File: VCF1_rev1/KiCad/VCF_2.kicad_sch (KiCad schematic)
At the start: 41 parts, among them U3 CEM3350, U4 Opamp_Quad, U5 74HC4053, U6 LM13700

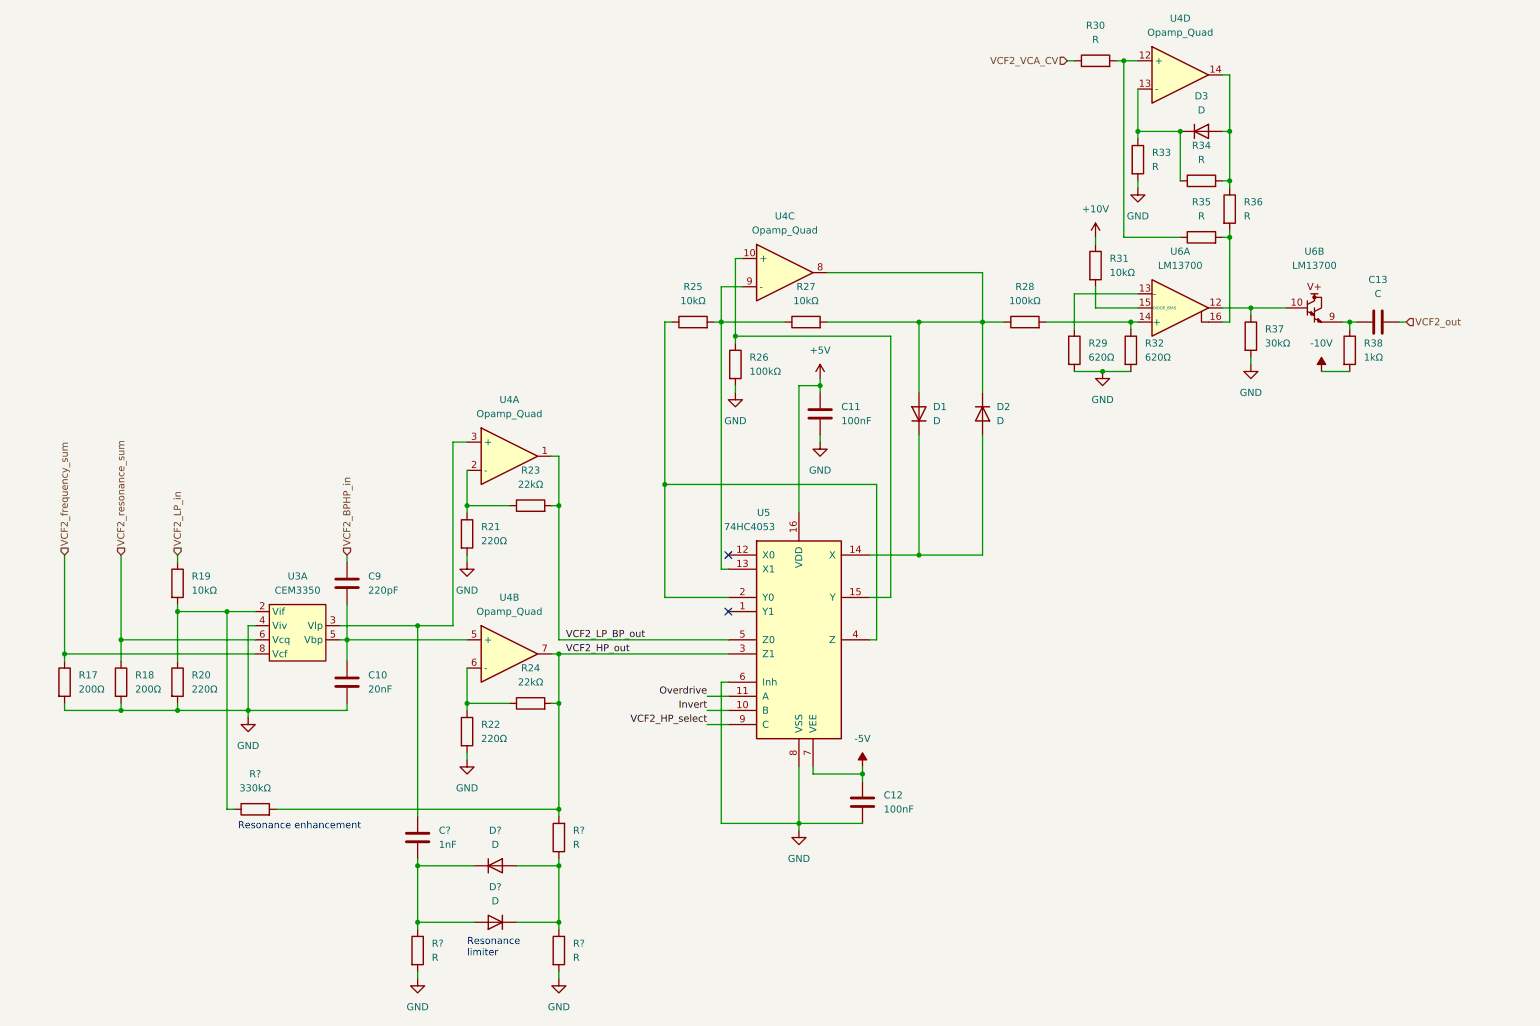
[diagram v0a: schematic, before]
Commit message: Added VCA (with a quirk) and also drew a new symbol for 74HC4053 because the standard one annoyed me.
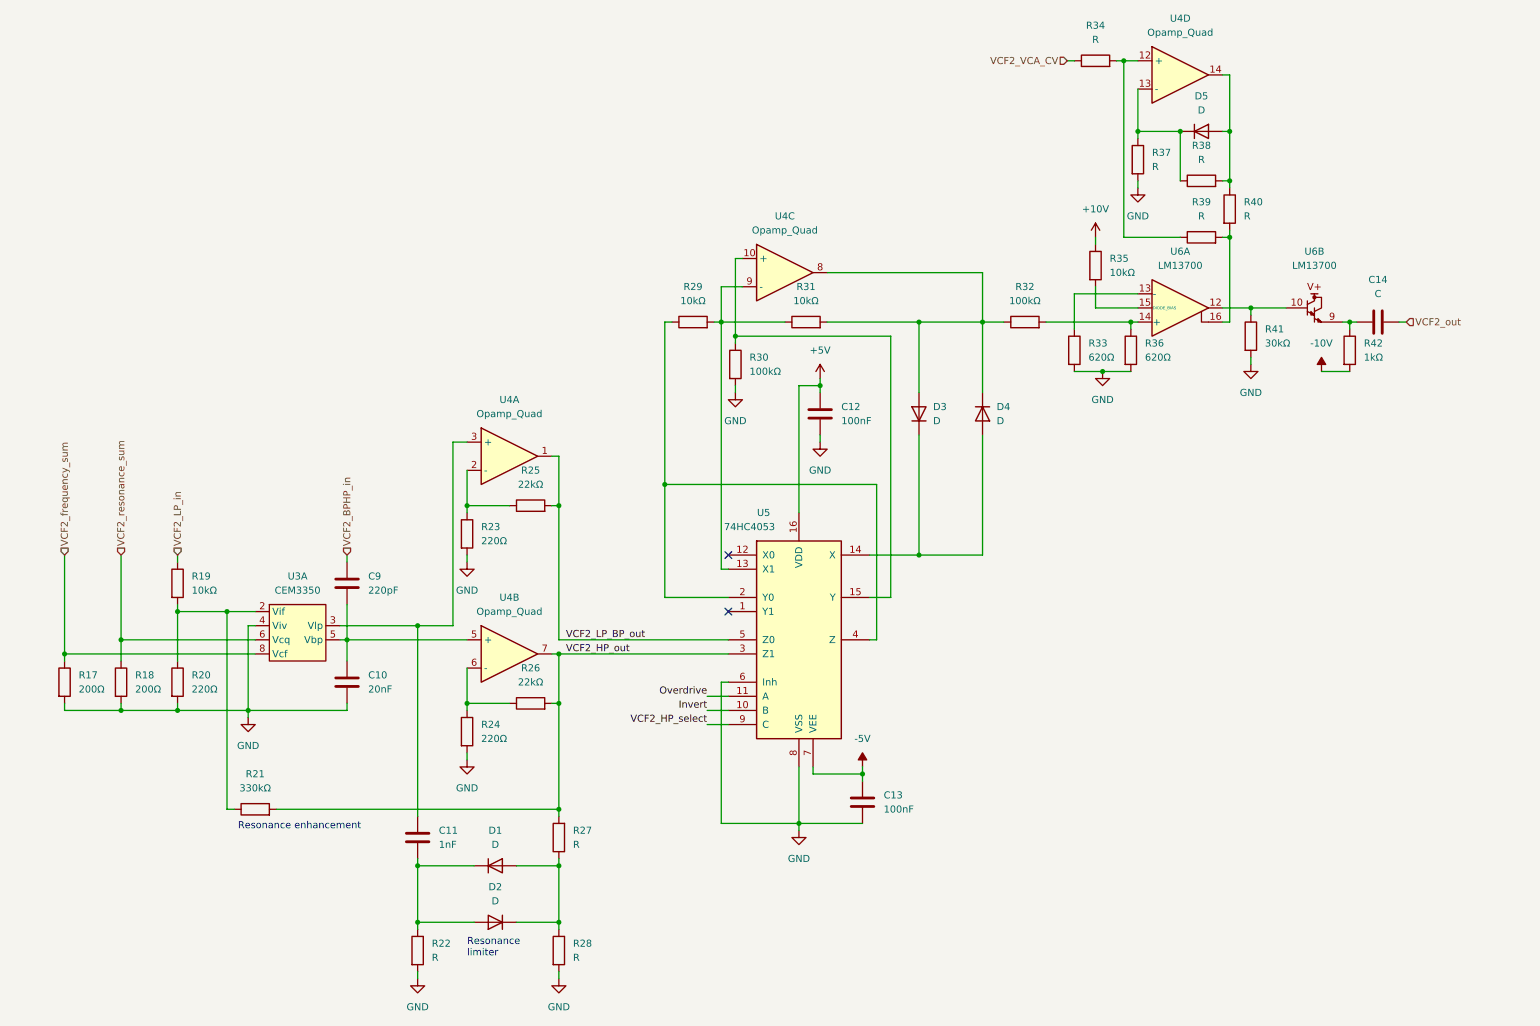
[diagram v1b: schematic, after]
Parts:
- gave numbers to parts that had none: 7
- renumbered C11 to C12, C12 to C13, C13 to C14, D1 to D3, D2 to D4, D3 to D5, R21 to R23, R22 to R24, R23 to R25, R24 to R26, R25 to R29, R26 to R30, R27 to R31, R28 to R32, R29 to R33, R30 to R34, R31 to R35, R32 to R36, R33 to R37, R34 to R38, R35 to R39, R36 to R40, R37 to R41, R38 to R42

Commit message: Cleaned up the VCF2 schematics.
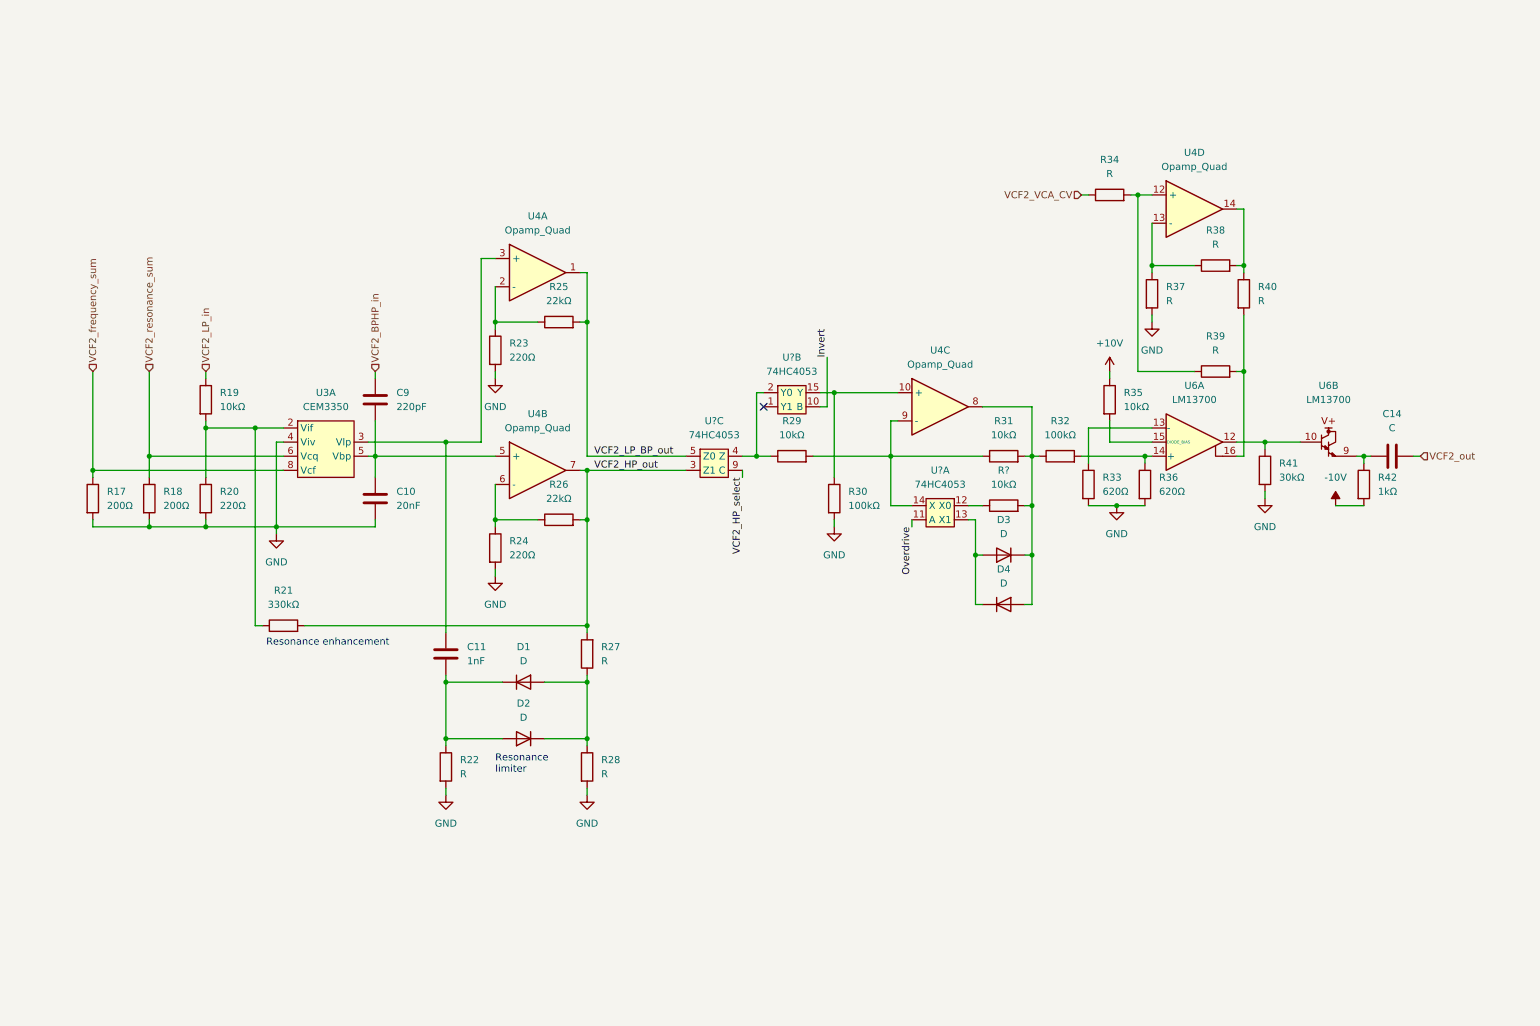
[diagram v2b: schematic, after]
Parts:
- removed C12, C13: 100nF, symbol Device:C
- removed D5: D, symbol Device:D
- removed U5: 74HC4053, symbol 4xxx:4053
- added R?: 10kΩ, symbol Device:R
- added U? (x3): 74HC4053, symbol Modular_Mayhem:74HC4053
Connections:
- net Invert: now also U?.10 (B)
- net Overdrive: now also U?.11 (A)
- net VCF2_HP_out: now also U?.3 (Z1)
- net VCF2_HP_select: now also U?.9 (C)
- net VCF2_LP_BP_out: now also U?.5 (Z0)
- net at R29.1: now also U?.2 (Y0), U?.4 (Z)
- net at R29.2, R31.1, U4.9 (-): now also U?.14 (X)
- net at R30.1, U4.10 (+): now also U?.15 (Y)
- net at R31.2, R32.1, U4.8: now also D3.1 (K), D4.2 (A), R?.2; no longer D3.2 (A), D4.1 (K)
- new net: R?.1, U?.12 (X0)
- new net: D3.2 (A), D4.1 (K), U?.13 (X1)
- no-connect marks 2 -> 1
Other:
- moved on the sheet: C10, C11, C14, C9, D1, D2, D3, D4, R17, R18, R19, R20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

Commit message: The filter blocks are more or less done, page order has gotten more sane for easier reading.
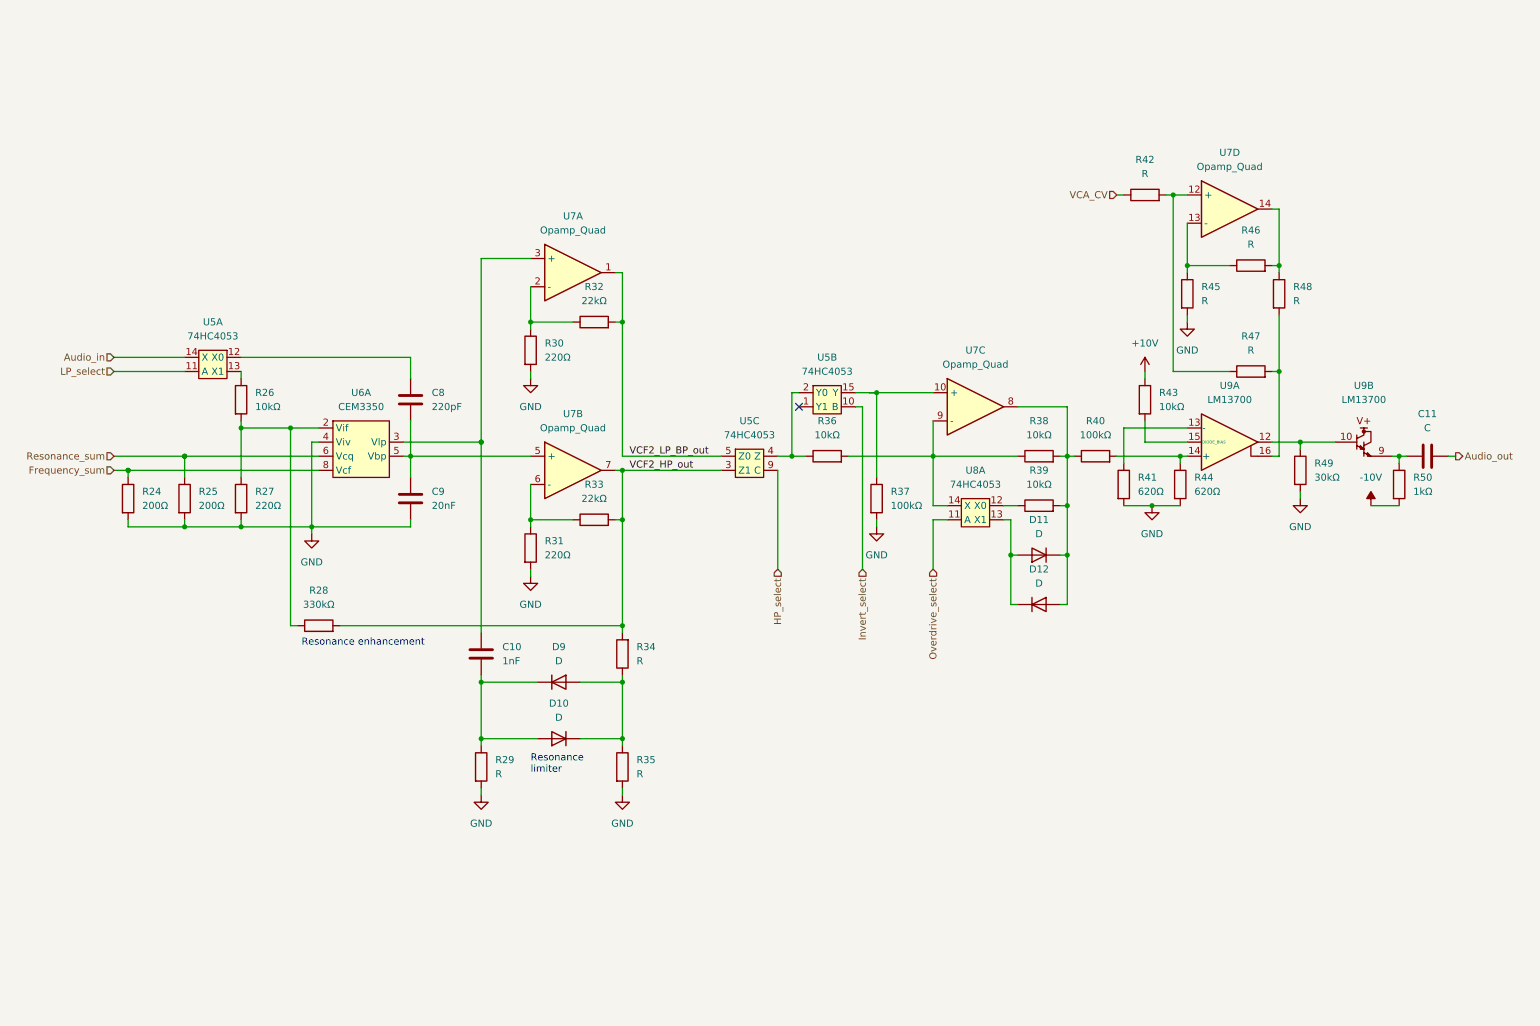
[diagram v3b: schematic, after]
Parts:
- added unit 1 of U5
- gave numbers to parts that had none: 3
- renumbered C11 to C10, C14 to C11, C9 to C8, C10 to C9, D2 to D10, D3 to D11, D4 to D12, D1 to D9, R17 to R24, R18 to R25, R19 to R26, R20 to R27, R21 to R28, R22 to R29, R23 to R30, R24 to R31, R25 to R32, R26 to R33, R27 to R34, R28 to R35, R29 to R36, R30 to R37, R31 to R38, R32 to R40, R33 to R41, R34 to R42, R35 to R43, R36 to R44, R37 to R45, R38 to R46, R39 to R47, R40 to R48, R41 to R49, R42 to R50, U3 to U6, U4 to U7, U6 to U9
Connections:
- net at R36.2, R38.1: no longer U7.9 (-), U8.14 (X)
- net Invert renamed Invert_select
- net Overdrive renamed Overdrive_select
- net VCF2_BPHP_in: no longer names the net of C8.1
- net VCF2_BPHP_in: now also U5.12 (X0)
- net VCF2_HP_select renamed HP_select
- net VCF2_LP_in: no longer names the net of R26.1
- net VCF2_LP_in: now also U5.13 (X1)
- net VCF2_VCA_CV renamed VCA_CV
- net VCF2_frequency_sum: no longer names the net of R24.1, U6.8 (Vcf)
- net VCF2_out renamed Audio_out
- net VCF2_resonance_sum: no longer names the net of R25.1, U6.6 (Vcq)
- new net: U7.9 (-), U8.14 (X)
- new net Audio_in: U5.14 (X)
- new net LP_select: U5.11 (A)
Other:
- moved on the sheet: C10, C11, C8, C9, D10, D11, D12, D9, R24, R25, R26, R27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

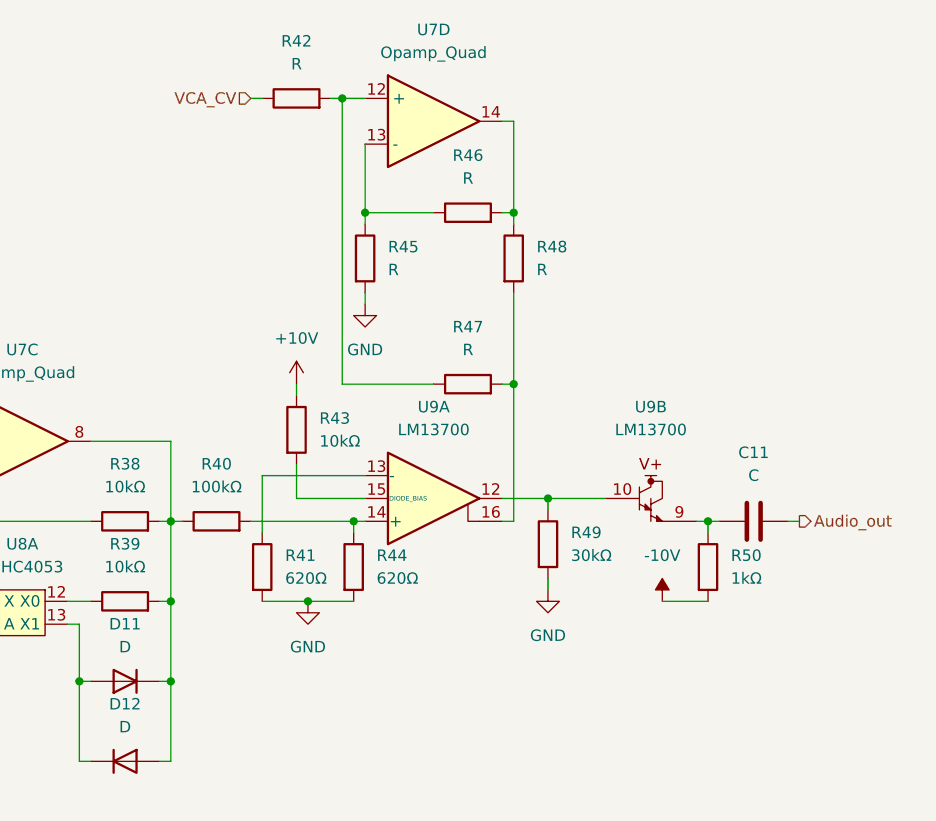
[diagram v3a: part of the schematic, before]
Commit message: Added the MUX. The signal path is now more or less complete!
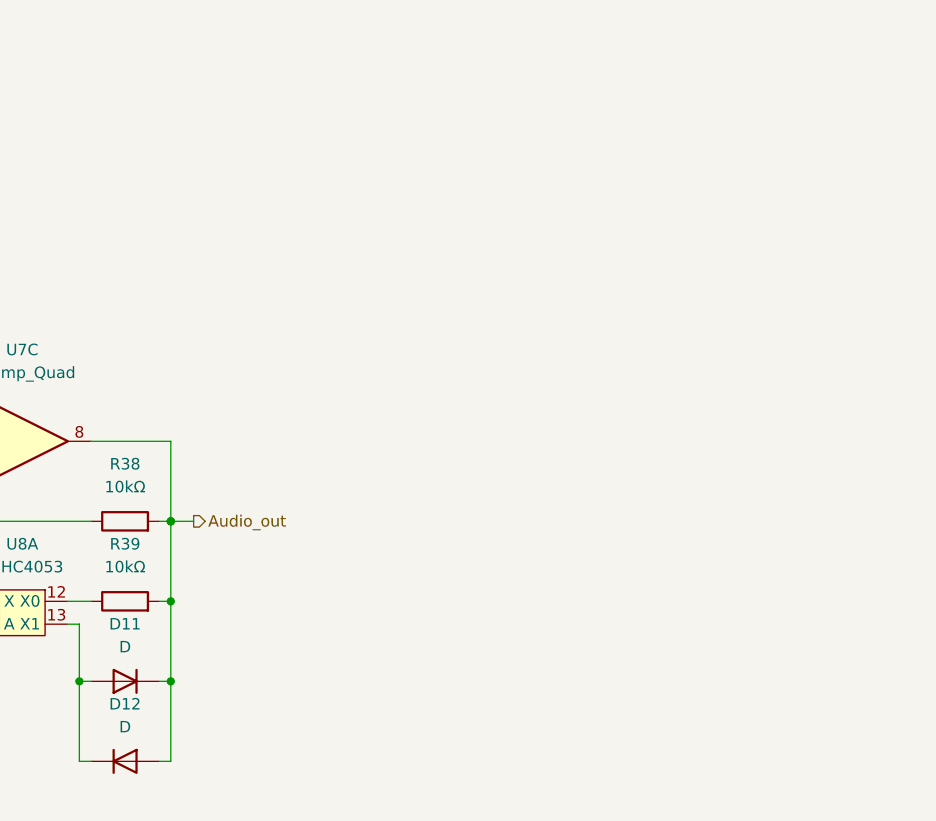
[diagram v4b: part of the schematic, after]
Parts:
- removed C11: C, symbol Device:C
- removed R40: 100kΩ, symbol Device:R
- removed R41, R44: 620Ω, symbol Device:R
- removed R42, R45, R46, R47, R48: R, symbol Device:R
- removed R43: 10kΩ, symbol Device:R
- removed R49: 30kΩ, symbol Device:R
- removed R50: 1kΩ, symbol Device:R
- removed unit 4 of U7
- removed U9: LM13700, symbol Amplifier_Operational:LM13700
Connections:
- net Audio_out: now also D11.1 (K), D12.2 (A), R38.2, R39.2, U7.8

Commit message: Lot of work on panel etc.
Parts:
- renumbered C9 to C10, C10 to C11, C8 to C9, R24 to R56, R25 to R57, R26 to R58, R27 to R59, R28 to R60, R29 to R61, R30 to R62, R31 to R63, R32 to R64, R33 to R65, R34 to R66, R35 to R67, R36 to R68, R37 to R69, R38 to R70, R39 to R71, U6 to U10, U7 to U11, U8 to U12, U5 to U9
